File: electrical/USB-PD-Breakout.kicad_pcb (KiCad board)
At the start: 2 copper layers, 50.8 x 25.4 mm, 18 parts, among them J1 USB-C_Female, J2 CONN_02X04, J3 USB_A, J4 CONN_01X05, J5 CONN_01X02, U1 FUSB302MPX

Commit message: Rev2 Update
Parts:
- removed G***: LOGO, Jason_Libraries:Reclaimer_Labs
- removed G***: LOGO, Jason_Libraries:Reclaimer_Labs_2mm
- removed R4: 4.7k, Jason_Libraries:R_0805
- added R1: 4.7k, Capacitors_SMD:C_0603, F.Cu at (129.5, 70.5)
- added X1: MTHOLE, Reclaimer_Labs:MountingHole_3.5mm_Pad_Via, F.Cu at (105.6, 97.6)
- added X2: MTHOLE, Reclaimer_Labs:MountingHole_3.5mm_Pad_Via, F.Cu at (105.6, 72.6)
- added X3: MTHOLE, Reclaimer_Labs:MountingHole_3.5mm_Pad_Via, F.Cu at (135.6, 72.6)
- added X4: MTHOLE, Reclaimer_Labs:MountingHole_3.5mm_Pad_Via, F.Cu at (135.6, 97.6)
- C1: value 22uF -> 10uF; footprint Jason_Libraries:R_0805 -> Capacitors_SMD:C_1206
- C2, C4, C5, C6: footprint Jason_Libraries:0603_np -> Capacitors_SMD:C_0603
- C3: footprint Jason_Libraries:R_0805 -> Capacitors_SMD:C_0805
- J1: footprint Jason_Libraries:USB-C_Female_Top_Mount_Dual_SMT_RA -> Reclaimer_Labs:USB-C_Female_105450-0101
- J2: value CONN_02X04 -> USB_OTG; footprint Socket_Strips:Socket_Strip_Straight_2x04 -> Reclaimer_Labs:USB_Micro-B_10118193
- J3: value USB_A -> CONN_02X03; footprint Jason_Libraries:USB_A_Female_SMD -> Socket_Strips:Socket_Strip_Straight_2x03
- J4: value CONN_01X05 -> CONN_02X03; footprint Socket_Strips:Socket_Strip_Straight_1x05 -> Socket_Strips:Socket_Strip_Straight_2x03
- J5: value CONN_01X02 -> CONN_02X03; footprint Socket_Strips:Socket_Strip_Straight_1x02 -> Socket_Strips:Socket_Strip_Straight_2x03
- R2, R3: footprint Jason_Libraries:R_0805 -> Capacitors_SMD:C_0603
- U1: value FUSB302MPX -> FUSB302BMPX; footprint Jason_Libraries:MLP_14 -> Reclaimer_Labs:MLP_14
- moved J5 60.5 mm to (121.3, 81.3), turned to 0 degrees
- moved C4 58.5 mm to (133.3, 92.7), turned to 0 degrees
- moved C3 58.4 mm to (133.3, 90.2), turned to 0 degrees
- moved C5 53.9 mm to (124.5, 94.6)
- moved C6 53.8 mm to (124.5, 90.8)
- moved R2 51.7 mm to (129.5, 72.4), turned to 180 degrees
- moved U1 49.0 mm to (128.3, 92.7), turned to 90 degrees
- moved R3 48.6 mm to (129.5, 74.3), turned to 180 degrees
- moved C2 44.7 mm to (121.9, 94.6), turned to 270 degrees
- moved C1 42.8 mm to (119.4, 95.2), turned to 270 degrees
- moved J1 42.6 mm to (105.7, 82.6)
- moved J4 42.4 mm to (110.5, 90.8)
- moved J2 36.3 mm to (115.6, 71.0)
- moved J3 35.4 mm to (134.0, 83.8), turned to 180 degrees
- moved REF** 28.7 mm to (114.9, 78.1)
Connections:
- net /CC1 renamed /USBC_CC1
- net /CC2 renamed /USBC_CC2
- C1 pad 1: /Vconn -> VCONN
- C2 pad 1: /Vconn -> VCONN
- C3 pad 1: /Vdd -> VDD
- C4 pad 1: /Vdd -> VDD
- J1 pad A4: /Vbus -> VBUS_C
- J1 pad A6: /D+ -> /USB20_D+
- J1 pad A7: /D- -> /USB20_D-
- J1 pad A9: /Vbus -> VBUS_C
- J1 pad B4: /Vbus -> VBUS_C
- J1 pad B6: /D+ -> /USB20_D+
- J1 pad B7: /D- -> /USB20_D-
- J1 pad B9: /Vbus -> VBUS_C
- J2 pad 1: /VbusA -> VBUS_A
- J2 pad 2: GND -> /USB20_D-
- J2 pad 3: /Vdd -> /USB20_D+
- J2 pad 4: GND -> Net-(J2-Pad4)
- J2 pad 5: /Vconn -> GND
- J2 pad 6: GND -> Net-(J2-Pad6)
- J2 pad 7: /Vbus -> (no net)
- J2 pad 8: GND -> (no net)
- J3 pad 1: /VbusA -> V_PULLUP
- J3 pad 2: /D- -> VDD
- J3 pad 3: /D+ -> /~INT
- J4 pad 1: /Vpu -> VBUS_C
- J4 pad 2: /~INT -> GND
- J4 pad 3: /SCL -> VBUS_C
- J4 pad 4: /SDA -> GND
- J4 pad 5: GND -> VCONN
- J5 pad 1: /Vpu -> V_PULLUP
- J5 pad 2: /Vbus -> VCONN
- R2 pad 1: /Vpu -> V_PULLUP
- R2 pad 2: /SDA -> /SCL
- R3 pad 1: /Vpu -> V_PULLUP
- R3 pad 2: /SCL -> /~INT
- U1 pad 12: /Vconn -> VCONN
- U1 pad 13: /Vconn -> VCONN
- U1 pad 2: /Vbus -> VBUS_C
- U1 pad 3: /Vdd -> VDD
- U1 pad 4: /Vdd -> VDD
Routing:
- net (no net): track 152.4 -> 0.00 mm
- net /D+: track 36.1 -> 0.00 mm, vias 2 -> 0
- net /D-: track 35.5 -> 0.00 mm, vias 3 -> 0
- net V_PULLUP: track 0.00 -> 32.9 mm, vias 0 -> 2
- net /Vbus: track 31.3 -> 0.00 mm, vias 4 -> 0
- net /Vdd: track 30.8 -> 0.00 mm, vias 2 -> 0
- net /Vpu: track 30.6 -> 0.00 mm, vias 1 -> 0
- net VBUS_C: track 0.00 -> 26.9 mm
- net VDD: track 0.00 -> 24.0 mm, vias 0 -> 8
- net /USB20_D-: track 0.00 -> 22.9 mm, vias 0 -> 2
- net GND: track 18.1 -> 40.9 mm, vias 13 -> 29
- net /USB20_D+: track 0.00 -> 20.7 mm, vias 0 -> 2
- net /VbusA: track 16.2 -> 0.00 mm
- net /USBC_CC2: track 19.6 -> 33.9 mm
- net /Vconn: track 13.6 -> 0.00 mm
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- added copper zone on F.Cu, net VBUS_A
- added copper zone on F.Cu, net VBUS_C
- added copper zone on F.Cu, net VCONN
- added copper zone on B.Cu, net VDD
- added copper zone on F.Cu, net VDD
- removed copper zone on F.Cu, net /Vbus
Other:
- board size 50.8 x 25.4 mm -> 38 x 33 mm
- net class Default: clearance 0.1524 -> 0.126746; trace_width 0.1524 -> 0.127; via_dia 0.5842 -> 0.762
- rule trace_clearance: 0.1524 -> 0.126746
- rule trace_min: 0.1524 -> 0.12446
- rule via_min_drill: 0.254 -> 0.3302
- rule via_min_size: 0.508 -> 0.762
- board text added: "INT"
- board text added: "USB PowerDelivery Breakout Rev 2 ReclaimerLabs.com"
- board text added: "VBUS"
- board text added: "VBUS_A"
- board text added: "VCONN"
- board text added: "VDD"
- board text added: "VPU"
- board text added: "V_PULLUP"
- board text removed: "Reclaimer Labs, LLC reclaimerlabs.com"
- board text removed: "USB Power Delivery Breakout Rev 1 01/20/2016"
- board text removed: "Vbus"
- board text removed: "VbusA"
- board text removed: "Vconn"
- board text removed: "Vdd"
- board text removed: "Vpu"
- board text removed: "~INT"

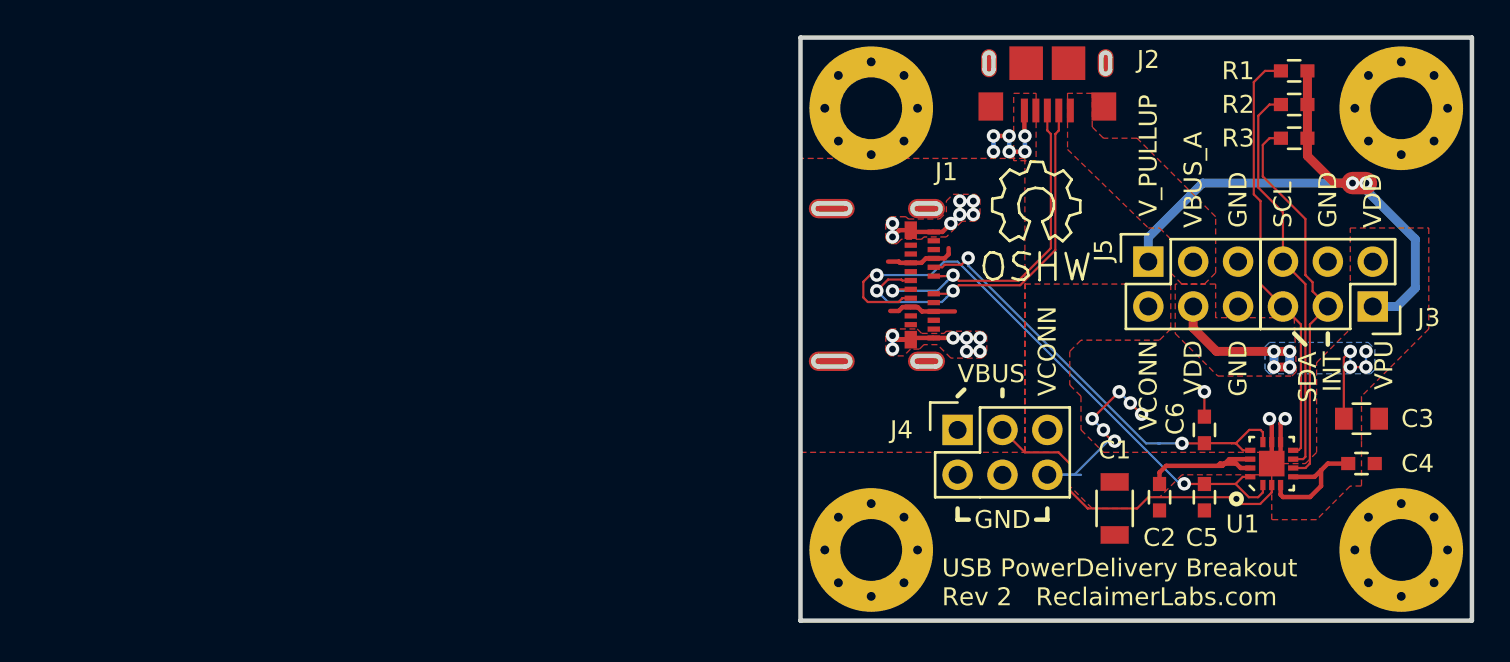
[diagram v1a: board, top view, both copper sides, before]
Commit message: Rev 4
Final Rev 4 design. Simplied headers, shrank board area, and added testpoints for DFM.
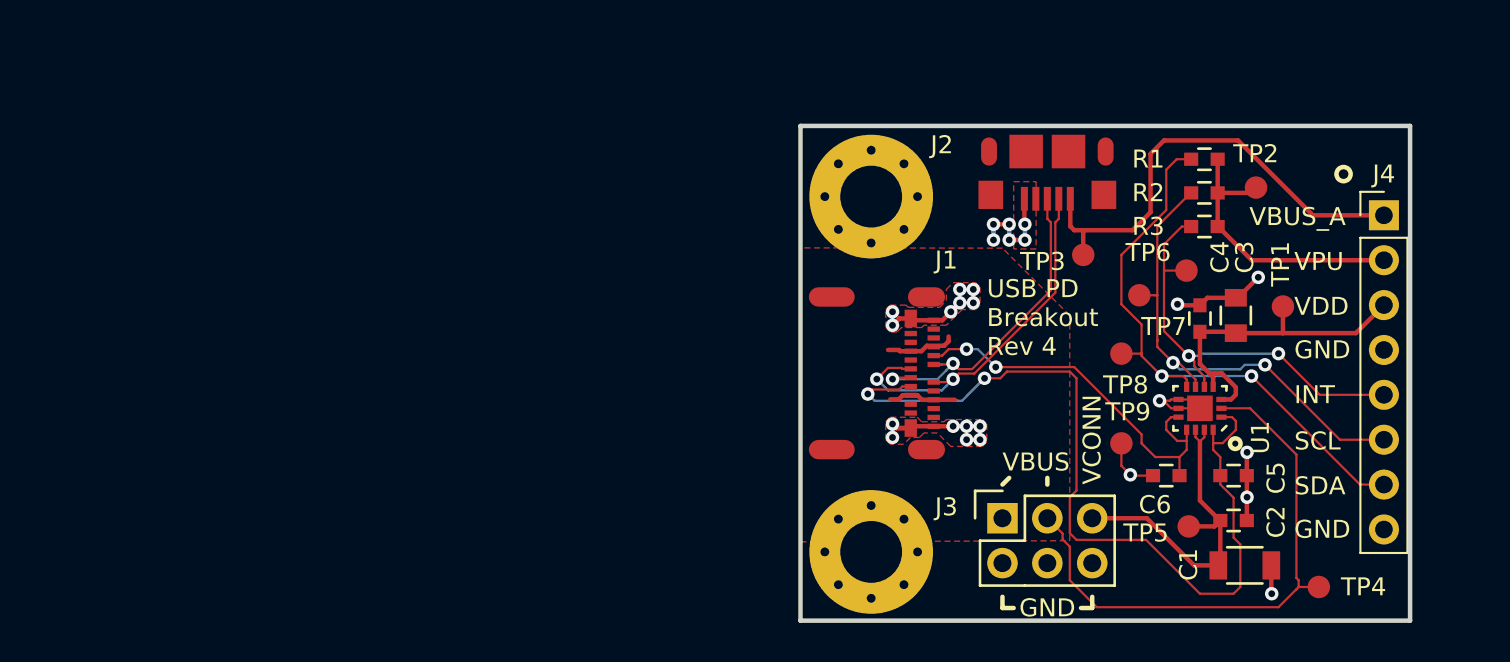
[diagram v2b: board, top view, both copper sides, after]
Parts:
- removed J5: CONN_02X03, Socket_Strips:Socket_Strip_Straight_2x03
- removed REF**: Symbol_OSHW-Logo_SilkScreen, Symbols:Symbol_OSHW-Logo_SilkScreen
- removed X3, X4: MTHOLE, Reclaimer_Labs:MountingHole_3.5mm_Pad_Via
- added TP1: TEST_1P, Jason_Custom_Home:TP, F.Cu at (128.9, 83.8)
- added TP2: TEST_1P, Jason_Custom_Home:TP, F.Cu at (127.4, 77.1)
- added TP3: TEST_1P, Jason_Custom_Home:TP, F.Cu at (117.6, 80.9)
- added TP4: TEST_1P, Jason_Custom_Home:TP, F.Cu at (130.9, 99.7)
- added TP5: TEST_1P, Jason_Custom_Home:TP, F.Cu at (123.6, 96.3)
- added TP6: TEST_1P, Jason_Custom_Home:TP, F.Cu at (123.4, 81.8)
- added TP7: TEST_1P, Jason_Custom_Home:TP, F.Cu at (120.8, 83.2)
- added TP8: TEST_1P, Jason_Custom_Home:TP, F.Cu at (119.8, 86.5)
- added TP9: TEST_1P, Jason_Custom_Home:TP, F.Cu at (119.8, 91.6)
- J4: value CONN_02X03 -> Conn_01x08_Male; footprint Socket_Strips:Socket_Strip_Straight_2x03 -> Socket_Strips:Socket_Strip_Straight_1x08_Pitch2.54mm
- moved J4 27.0 mm to (134.6, 78.7)
- moved J3 24.1 mm to (113.0, 95.8), turned to 0 degrees
- moved C4 12.3 mm to (124.2, 84.5), turned to 90 degrees
- moved C3 9.20 mm to (126.2, 84.3), turned to 90 degrees
- moved C1 8.04 mm to (126.7, 98.5), turned to 0 degrees
- moved R1 7.13 mm to (124.5, 75.5)
- moved R2 7.13 mm to (124.5, 77.4)
- moved R3 7.13 mm to (124.5, 79.3)
- moved U1 5.13 mm to (124.2, 89.6), turned to 180 degrees
- moved J1 5.00 mm to (105.7, 87.6)
- moved J2 5.00 mm to (115.6, 76.0)
- moved X2 5.00 mm to (105.6, 77.6)
- moved C2 4.39 mm to (126.1, 95.9), turned to 0 degrees
- moved C6 3.37 mm to (122.3, 93.4), turned to 180 degrees
- moved C5 2.05 mm to (126.1, 93.4), turned to 0 degrees
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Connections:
- J3 pad 1: V_PULLUP -> VBUS_C
- J3 pad 2: VDD -> GND
- J3 pad 3: /~INT -> VBUS_C
- J3 pad 5: /SDA -> VCONN
- J3 pad 6: /SCL -> GND
- J4 pad 1: VBUS_C -> VBUS_A
- J4 pad 2: GND -> V_PULLUP
- J4 pad 3: VBUS_C -> VDD
- J4 pad 5: VCONN -> /~INT
- J4 pad 6: GND -> /SCL
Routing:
- net VBUS_A: track 0.00 -> 26.6 mm
- net V_PULLUP: track 32.9 -> 16.3 mm, vias 2 -> 0
- net /USBC_CC2: track 33.9 -> 49.5 mm
- net VBUS_C: track 26.9 -> 39.9 mm
- net VCONN: track 8.09 -> 19.3 mm
- net /SDA: track 24.2 -> 33.5 mm, vias 0 -> 2
- net /SCL: track 22.7 -> 27.9 mm, vias 0 -> 2
- net VDD: track 24.0 -> 19.2 mm, vias 8 -> 0
- net /USBC_CC1: track 25.7 -> 22.3 mm
- net /~INT: track 22.2 -> 24.3 mm, vias 0 -> 2
- net /USB20_D+: track 20.7 -> 19.2 mm
- net /USB20_D-: track 22.9 -> 21.3 mm
- net GND: track 40.9 -> 40.6 mm, vias 29 -> 27
- removed copper zone on F.Cu, net VBUS_A
- removed copper zone on F.Cu, net VCONN
- removed copper zone on B.Cu, net VDD
- removed copper zone on F.Cu, net VDD
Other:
- board size 38 x 33 mm -> 34.5 x 28 mm
- board text added: "USB PD Breakout Rev 4"
- board text added: "USB PowerDelivery Breakout Board Rev 4 ReclaimerLabs.com"
- board text removed: "USB PowerDelivery Breakout Rev 2 ReclaimerLabs.com"
- board text removed: "V_PULLUP"
